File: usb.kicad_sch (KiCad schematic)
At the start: 9 parts

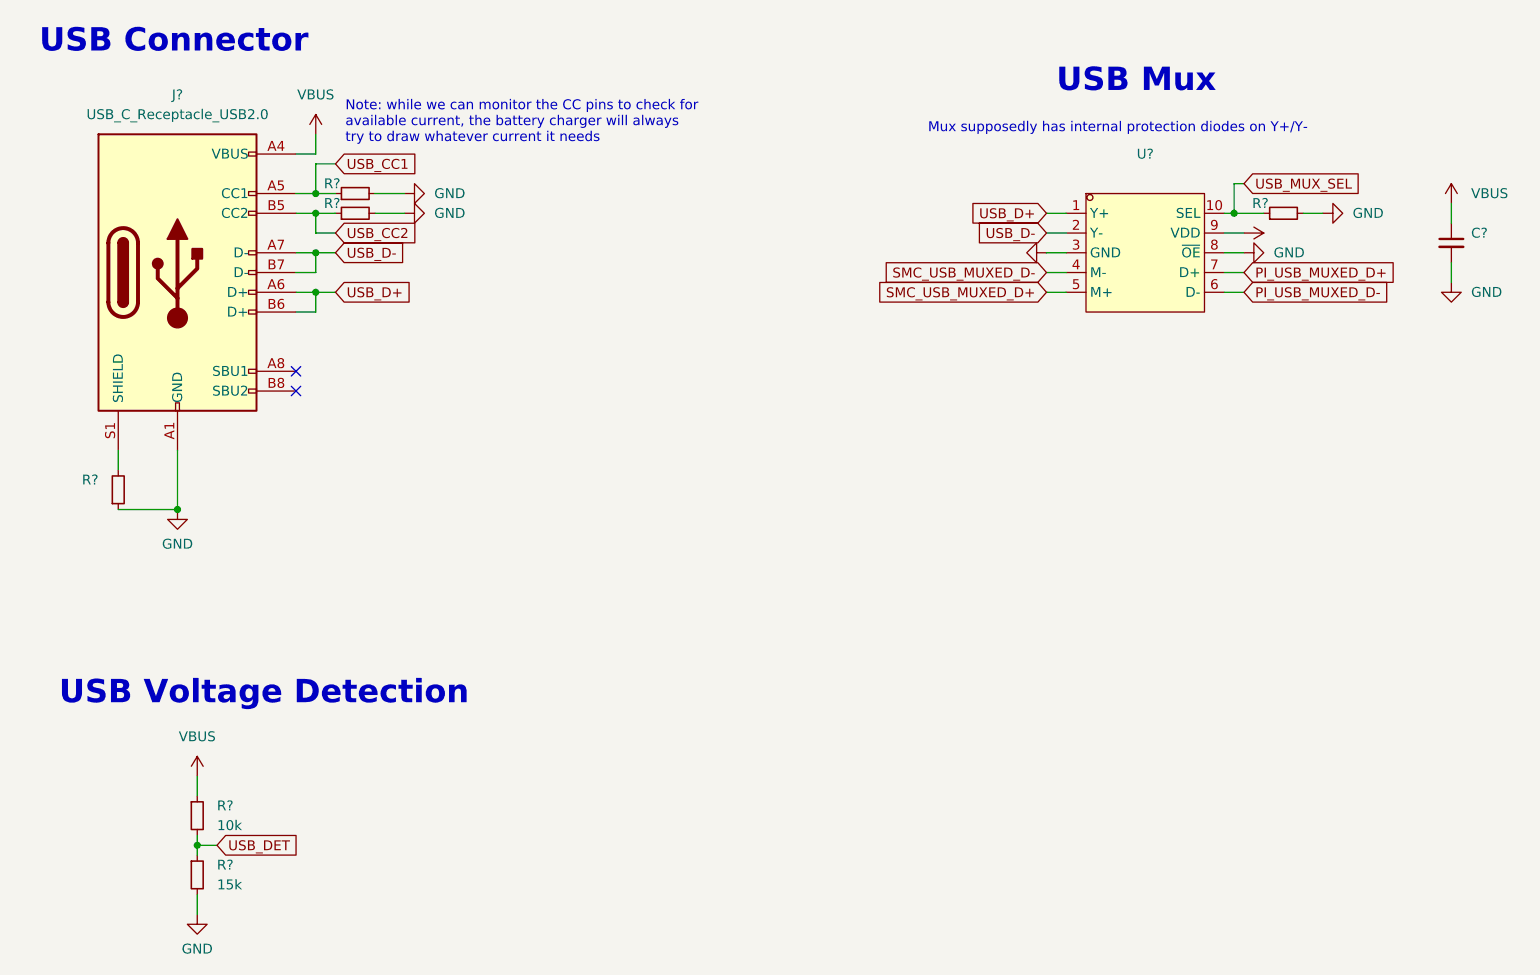
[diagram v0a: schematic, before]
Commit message: schem: first pass done, ERC passing
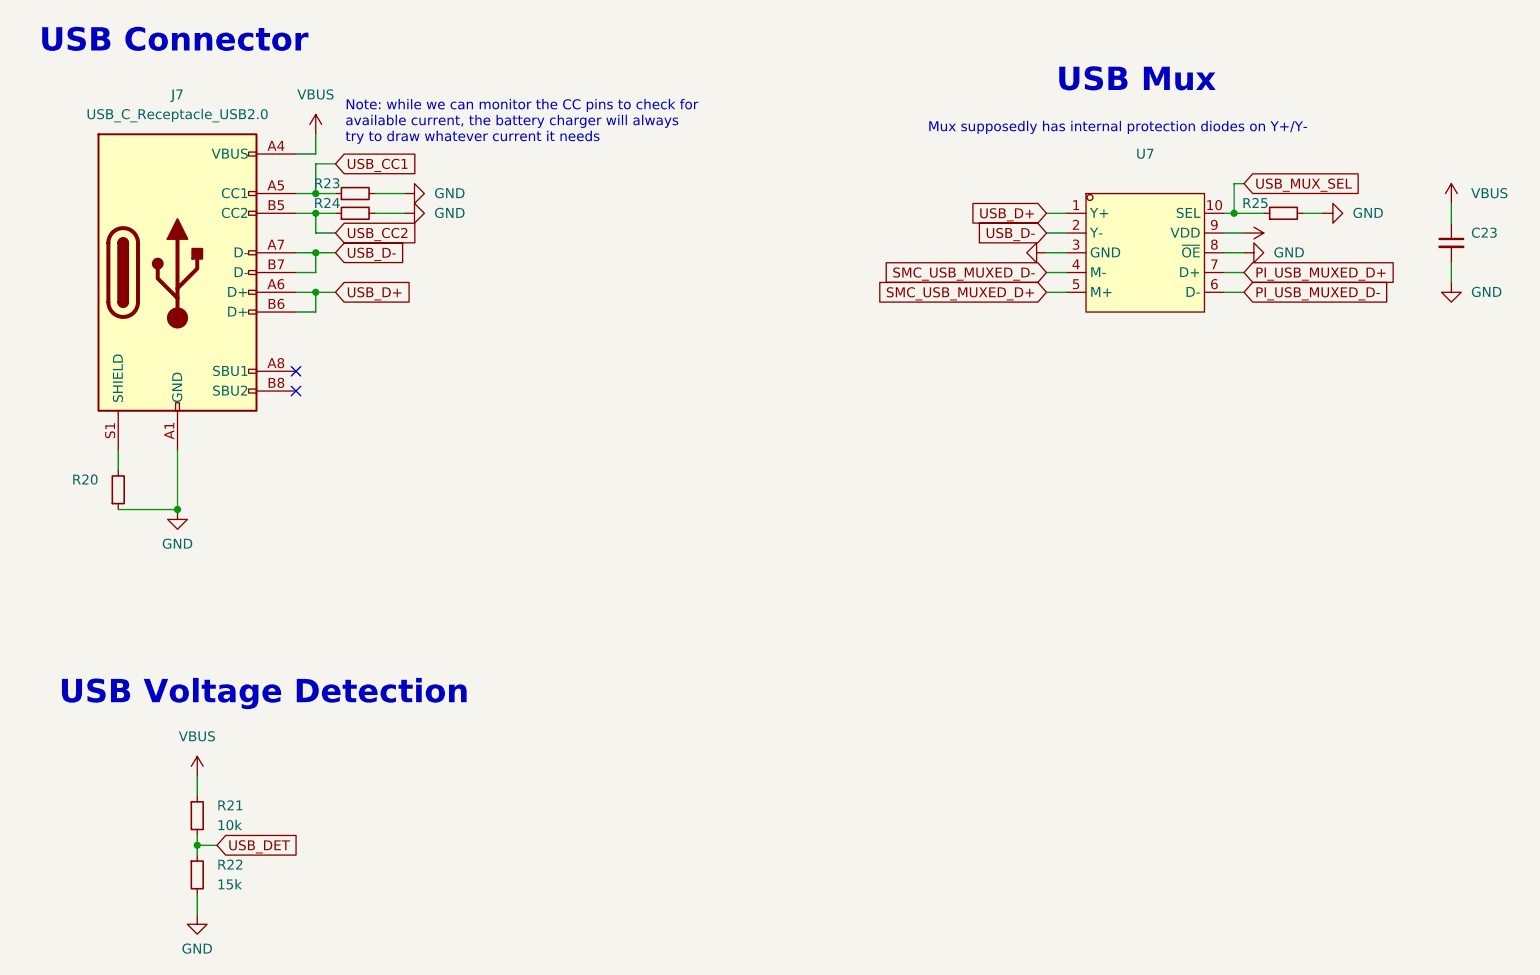
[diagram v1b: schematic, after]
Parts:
- gave numbers to parts that had none: 9
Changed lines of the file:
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@@
   (junction (at 63.5 110.49) (diameter 0) (color 0 0 0 0)
   )
+  (no_connect (at 78.74 95.25))
   (no_connect (at 78.74 92.71))
-  (no_connect (at 78.74 95.25))
   (wire (pts (xy 199.39 72.39) (xy 203.2 72.39))
     (stroke (width 0) (type default) (color 0 0 0 0))
@@
   (symbol (lib_id "power:GND") (at 66.04 162.56 0) (unit 1)
     (in_bom yes) (on_board yes) (fields_autoplaced)
-    (property "Reference" "#PWR?" (id 0) (at 66.04 168.91 0)
+    (property "Reference" "#PWR051" (id 0) (at 66.04 168.91 0)
       (effects (font (size 1.27 1.27)) hide)
     )
@@
   (symbol (lib_id "Device:R_Small") (at 66.04 157.48 0) (unit 1)
     (in_bom yes) (on_board yes) (fields_autoplaced)
-    (property "Reference" "R?" (id 0) (at 68.58 156.2099 0)
+    (property "Reference" "R22" (id 0) (at 68.58 156.2099 0)
       (effects (font (size 1.27 1.27)) (justify left))
     )
@@
   (symbol (lib_id "Device:R_Small") (at 66.04 149.86 0) (unit 1)
     (in_bom yes) (on_board yes) (fields_autoplaced)
-    (property "Reference" "R?" (id 0) (at 68.58 148.5899 0)
+    (property "Reference" "R21" (id 0) (at 68.58 148.5899 0)
       (effects (font (size 1.27 1.27)) (justify left))
     )
@@
   (symbol (lib_id "power:VBUS") (at 66.04 144.78 0) (unit 1)
     (in_bom yes) (on_board yes) (fields_autoplaced)
-    (property "Reference" "#PWR?" (id 0) (at 66.04 148.59 0)
+    (property "Reference" "#PWR050" (id 0) (at 66.04 148.59 0)
       (effects (font (size 1.27 1.27)) hide)
     )
@@
   (symbol (lib_id "power:VBUS") (at 227.33 71.12 0) (unit 1)
     (in_bom yes) (on_board yes) (fields_autoplaced)
-    (property "Reference" "#PWR?" (id 0) (at 227.33 74.93 0)
+    (property "Reference" "#PWR059" (id 0) (at 227.33 74.93 0)
       (effects (font (size 1.27 1.27)) hide)
     )
@@
   (symbol (lib_id "Device:R_Small") (at 86.36 69.85 90) (unit 1)
     (in_bom yes) (on_board yes)
-    (property "Reference" "R?" (id 0) (at 84.455 68.58 90)
+    (property "Reference" "R23" (id 0) (at 84.455 68.58 90)
       (effects (font (size 1.27 1.27)) (justify left))
     )
@@
   (symbol (lib_id "lcsc:PI3USB102EZLEX") (at 187.96 77.47 0) (unit 1)
     (in_bom yes) (on_board yes) (fields_autoplaced)
-    (property "Reference" "U?" (id 0) (at 187.96 64.77 0))
+    (property "Reference" "U7" (id 0) (at 187.96 64.77 0))
     (property "Value" "" (id 1) (at 187.96 67.31 0))
     (property "Footprint" "lcsc:TQFN-10_L1.6-W1.3-P0.50-BL" (id 2) (at 187.96 90.17 0)
@@
   (symbol (lib_id "power:GND") (at 175.26 77.47 270) (unit 1)
     (in_bom yes) (on_board yes) (fields_autoplaced)
-    (property "Reference" "#PWR?" (id 0) (at 168.91 77.47 0)
+    (property "Reference" "#PWR055" (id 0) (at 168.91 77.47 0)
       (effects (font (size 1.27 1.27)) hide)
     )
@@
   (symbol (lib_id "Device:C_Small") (at 227.33 76.2 0) (unit 1)
     (in_bom yes) (on_board yes) (fields_autoplaced)
-    (property "Reference" "C?" (id 0) (at 229.87 74.9362 0)
+    (property "Reference" "C23" (id 0) (at 229.87 74.9362 0)
       (effects (font (size 1.27 1.27)) (justify left))
     )
@@
   (symbol (lib_id "power:VBUS") (at 81.28 62.23 0) (unit 1)
     (in_bom yes) (on_board yes) (fields_autoplaced)
-    (property "Reference" "#PWR?" (id 0) (at 81.28 66.04 0)
+    (property "Reference" "#PWR052" (id 0) (at 81.28 66.04 0)
       (effects (font (size 1.27 1.27)) hide)
     )
@@
   (symbol (lib_id "Device:R_Small") (at 205.74 72.39 90) (unit 1)
     (in_bom yes) (on_board yes)
-    (property "Reference" "R?" (id 0) (at 203.835 71.12 90)
+    (property "Reference" "R25" (id 0) (at 203.835 71.12 90)
       (effects (font (size 1.27 1.27)) (justify left))
     )
@@
   (symbol (lib_id "power:GND") (at 92.71 69.85 90) (unit 1)
     (in_bom yes) (on_board yes) (fields_autoplaced)
-    (property "Reference" "#PWR?" (id 0) (at 99.06 69.85 0)
+    (property "Reference" "#PWR053" (id 0) (at 99.06 69.85 0)
       (effects (font (size 1.27 1.27)) hide)
     )
@@
   (symbol (lib_id "power:GND") (at 92.71 72.39 90) (unit 1)
     (in_bom yes) (on_board yes) (fields_autoplaced)
-    (property "Reference" "#PWR?" (id 0) (at 99.06 72.39 0)
+    (property "Reference" "#PWR054" (id 0) (at 99.06 72.39 0)
       (effects (font (size 1.27 1.27)) hide)
     )
@@
   (symbol (lib_id "Device:R_Small") (at 86.36 72.39 90) (unit 1)
     (in_bom yes) (on_board yes)
-    (property "Reference" "R?" (id 0) (at 84.455 71.12 90)
+    (property "Reference" "R24" (id 0) (at 84.455 71.12 90)
       (effects (font (size 1.27 1.27)) (justify left))
     )
@@
   (symbol (lib_id "power:GND") (at 227.33 81.28 0) (unit 1)
     (in_bom yes) (on_board yes) (fields_autoplaced)
-    (property "Reference" "#PWR?" (id 0) (at 227.33 87.63 0)
+    (property "Reference" "#PWR060" (id 0) (at 227.33 87.63 0)
       (effects (font (size 1.27 1.27)) hide)
     )
@@
   (symbol (lib_id "power:GND") (at 200.66 77.47 90) (unit 1)
     (in_bom yes) (on_board yes) (fields_autoplaced)
-    (property "Reference" "#PWR?" (id 0) (at 207.01 77.47 0)
+    (property "Reference" "#PWR057" (id 0) (at 207.01 77.47 0)
       (effects (font (size 1.27 1.27)) hide)
     )
@@
   (symbol (lib_id "power:GND") (at 63.5 110.49 0) (unit 1)
     (in_bom yes) (on_board yes) (fields_autoplaced)
-    (property "Reference" "#PWR?" (id 0) (at 63.5 116.84 0)
+    (property "Reference" "#PWR049" (id 0) (at 63.5 116.84 0)
       (effects (font (size 1.27 1.27)) hide)
     )
@@
   (symbol (lib_id "power:GND") (at 210.82 72.39 90) (unit 1)
     (in_bom yes) (on_board yes) (fields_autoplaced)
-    (property "Reference" "#PWR?" (id 0) (at 217.17 72.39 0)
+    (property "Reference" "#PWR058" (id 0) (at 217.17 72.39 0)
       (effects (font (size 1.27 1.27)) hide)
     )
@@
   (symbol (lib_id "Connector:USB_C_Receptacle_USB2.0") (at 63.5 80.01 0) (unit 1)
     (in_bom yes) (on_board yes) (fields_autoplaced)
-    (property "Reference" "J?" (id 0) (at 63.5 57.15 0))
+    (property "Reference" "J7" (id 0) (at 63.5 57.15 0))
     (property "Value" "USB_C_Receptacle_USB2.0" (id 1) (at 63.5 59.69 0))
     (property "Footprint" "Gigahawk:USB_C_Receptacle_GCT_USB4085" (id 2) (at 67.31 80.01 0)
@@
   (symbol (lib_id "Device:R_Small") (at 55.88 107.95 0) (mirror x) (unit 1)
     (in_bom yes) (on_board yes) (fields_autoplaced)
-    (property "Reference" "R?" (id 0) (at 53.34 106.6799 0)
+    (property "Reference" "R20" (id 0) (at 53.34 106.6799 0)
       (effects (font (size 1.27 1.27)) (justify right))
     )
@@
   (symbol (lib_id "power:VBUS") (at 200.66 74.93 270) (unit 1)
     (in_bom yes) (on_board yes) (fields_autoplaced)
-    (property "Reference" "#PWR?" (id 0) (at 196.85 74.93 0)
-      (effects (font (size 1.27 1.27)) hide)
-    )
+    (property "Reference" "#PWR056" (id 0) (at 196.85 74.93 0)
+      (effects (font (size 1.27 1.27)) hide)
+    )

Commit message: analysis: specify pi will be powered directly from VCC
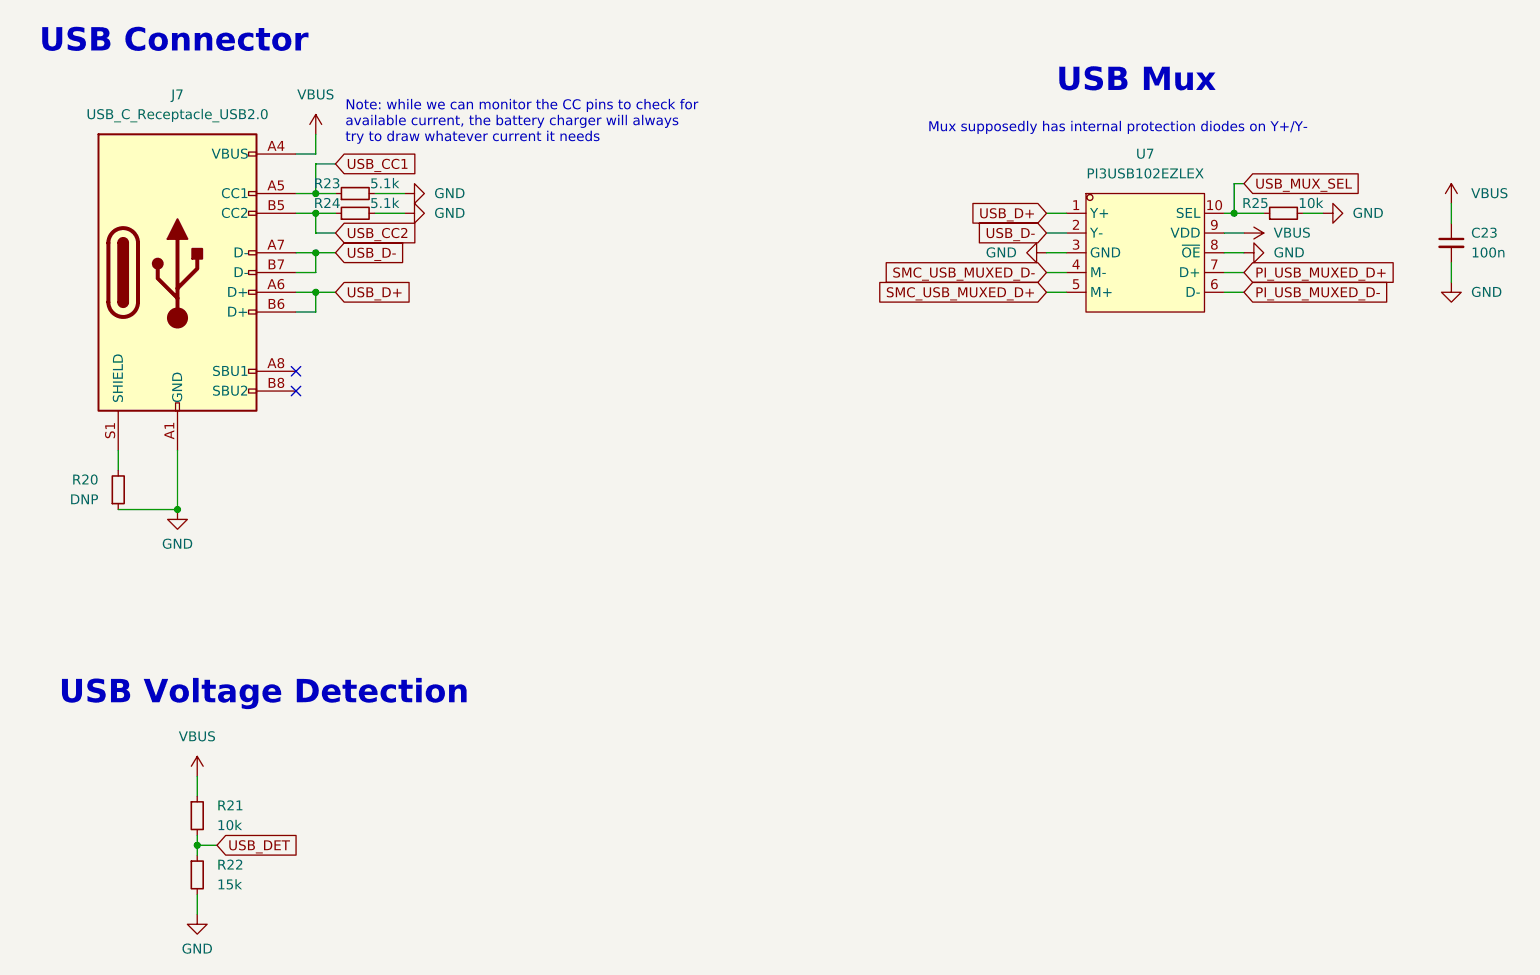
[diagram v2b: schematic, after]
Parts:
- C23: value (none) -> 100n; footprint (none) -> Capacitor_SMD:C_0402_1005Metric
- R20: value (none) -> DNP; footprint (none) -> Resistor_SMD:R_0402_1005Metric
- R21, R22: footprint (none) -> Resistor_SMD:R_0402_1005Metric
- R23, R24: value (none) -> 5.1k; footprint (none) -> Resistor_SMD:R_0402_1005Metric
- R25: value (none) -> 10k; footprint (none) -> Resistor_SMD:R_0402_1005Metric
- U7: value (none) -> PI3USB102EZLEX
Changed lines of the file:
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@@
       (effects (font (size 1.27 1.27)) (justify left))
     )
-    (property "Footprint" "" (id 2) (at 66.04 157.48 0)
+    (property "Footprint" "Resistor_SMD:R_0402_1005Metric" (id 2) (at 66.04 157.48 0)
       (effects (font (size 1.27 1.27)) hide)
     )
@@
       (effects (font (size 1.27 1.27)) (justify left))
     )
-    (property "Footprint" "" (id 2) (at 66.04 149.86 0)
+    (property "Footprint" "Resistor_SMD:R_0402_1005Metric" (id 2) (at 66.04 149.86 0)
       (effects (font (size 1.27 1.27)) hide)
     )
@@
       (effects (font (size 1.27 1.27)) (justify left))
     )
-    (property "Value" "" (id 1) (at 88.265 68.58 90)
-      (effects (font (size 1.27 1.27)) (justify right))
-    )
-    (property "Footprint" "" (id 2) (at 86.36 69.85 0)
+    (property "Value" "5.1k" (id 1) (at 88.265 68.58 90)
+      (effects (font (size 1.27 1.27)) (justify right))
+    )
+    (property "Footprint" "Resistor_SMD:R_0402_1005Metric" (id 2) (at 86.36 69.85 0)
       (effects (font (size 1.27 1.27)) hide)
     )
@@
     (in_bom yes) (on_board yes) (fields_autoplaced)
     (property "Reference" "U7" (id 0) (at 187.96 64.77 0))
-    (property "Value" "" (id 1) (at 187.96 67.31 0))
+    (property "Value" "PI3USB102EZLEX" (id 1) (at 187.96 67.31 0))
     (property "Footprint" "lcsc:TQFN-10_L1.6-W1.3-P0.50-BL" (id 2) (at 187.96 90.17 0)
       (effects (font (size 1.27 1.27)) hide)
@@
       (effects (font (size 1.27 1.27)) hide)
     )
-    (property "Value" "" (id 1) (at 171.45 77.4699 90)
+    (property "Value" "GND" (id 1) (at 171.45 77.4699 90)
       (effects (font (size 1.27 1.27)) (justify right))
     )
@@
       (effects (font (size 1.27 1.27)) (justify left))
     )
-    (property "Value" "" (id 1) (at 229.87 77.4762 0)
-      (effects (font (size 1.27 1.27)) (justify left))
-    )
-    (property "Footprint" "" (id 2) (at 227.33 76.2 0)
+    (property "Value" "100n" (id 1) (at 229.87 77.4762 0)
+      (effects (font (size 1.27 1.27)) (justify left))
+    )
+    (property "Footprint" "Capacitor_SMD:C_0402_1005Metric" (id 2) (at 227.33 76.2 0)
       (effects (font (size 1.27 1.27)) hide)
     )
@@
       (effects (font (size 1.27 1.27)) (justify left))
     )
-    (property "Value" "" (id 1) (at 207.645 71.12 90)
-      (effects (font (size 1.27 1.27)) (justify right))
-    )
-    (property "Footprint" "" (id 2) (at 205.74 72.39 0)
+    (property "Value" "10k" (id 1) (at 207.645 71.12 90)
+      (effects (font (size 1.27 1.27)) (justify right))
+    )
+    (property "Footprint" "Resistor_SMD:R_0402_1005Metric" (id 2) (at 205.74 72.39 0)
       (effects (font (size 1.27 1.27)) hide)
     )
@@
       (effects (font (size 1.27 1.27)) (justify left))
     )
-    (property "Value" "" (id 1) (at 88.265 71.12 90)
-      (effects (font (size 1.27 1.27)) (justify right))
-    )
-    (property "Footprint" "" (id 2) (at 86.36 72.39 0)
+    (property "Value" "5.1k" (id 1) (at 88.265 71.12 90)
+      (effects (font (size 1.27 1.27)) (justify right))
+    )
+    (property "Footprint" "Resistor_SMD:R_0402_1005Metric" (id 2) (at 86.36 72.39 0)
       (effects (font (size 1.27 1.27)) hide)
     )
@@
       (effects (font (size 1.27 1.27)) (justify right))
     )
-    (property "Value" "" (id 1) (at 53.34 109.2199 0)
-      (effects (font (size 1.27 1.27)) (justify right))
-    )
-    (property "Footprint" "" (id 2) (at 55.88 107.95 0)
+    (property "Value" "DNP" (id 1) (at 53.34 109.2199 0)
+      (effects (font (size 1.27 1.27)) (justify right))
+    )
+    (property "Footprint" "Resistor_SMD:R_0402_1005Metric" (id 2) (at 55.88 107.95 0)
       (effects (font (size 1.27 1.27)) hide)
     )
@@
       (effects (font (size 1.27 1.27)) hide)
     )
-    (property "Value" "" (id 1) (at 204.47 74.9299 90)
-      (effects (font (size 1.27 1.27)) (justify left))
-    )
+    (property "Value" "VBUS" (id 1) (at 204.47 74.9299 90)
+      (effects (font (size 1.27 1.27)) (justify left))
+    )
